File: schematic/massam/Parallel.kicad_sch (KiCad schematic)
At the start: 3 parts, among them J200 Conn_02x40_Row_Letter_First, U300 82C55A

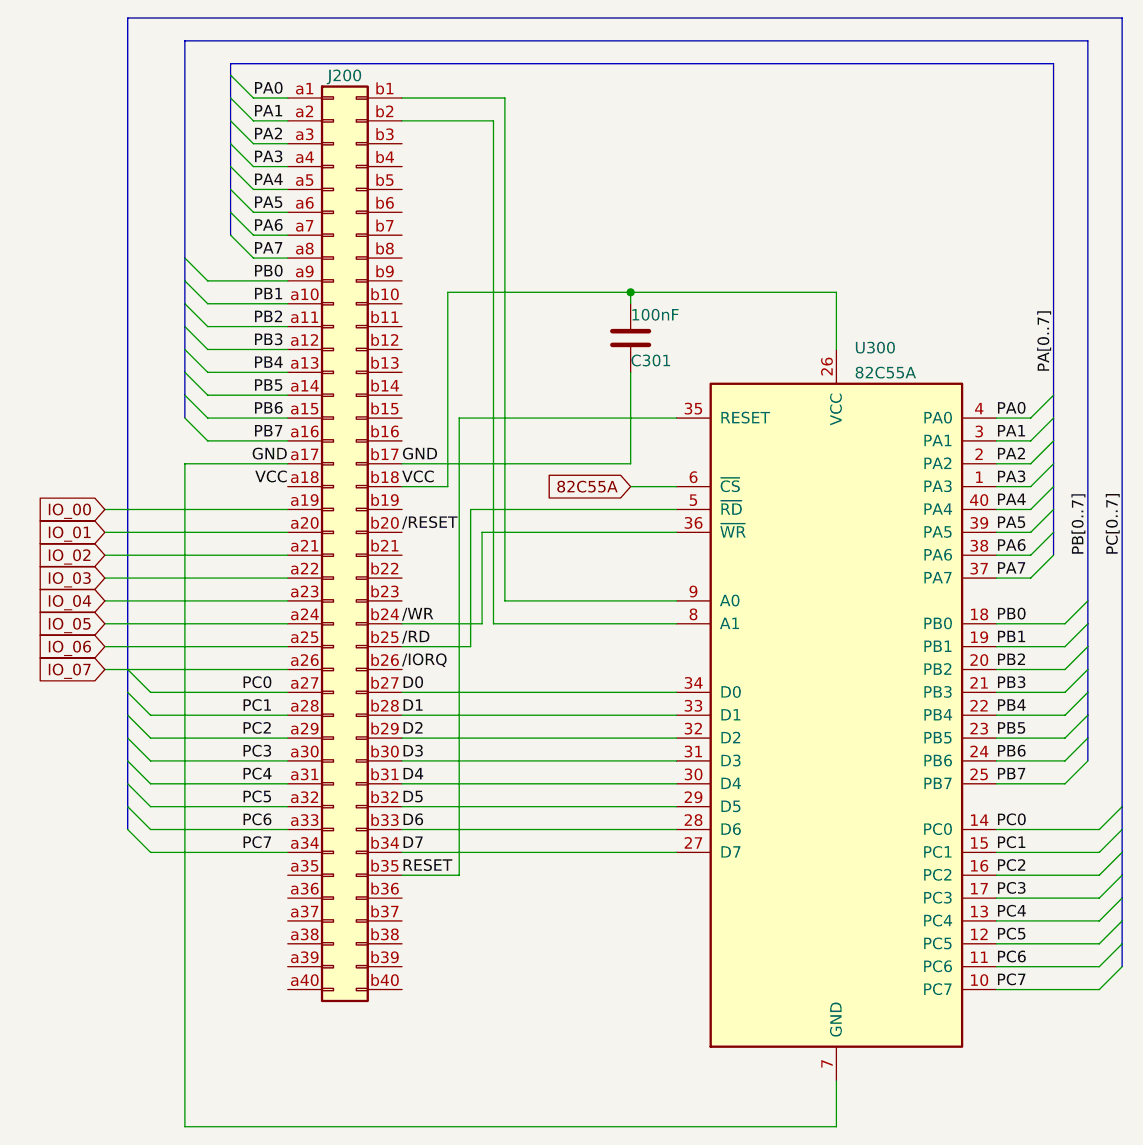
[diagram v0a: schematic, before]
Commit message: Added schematic for W65C02
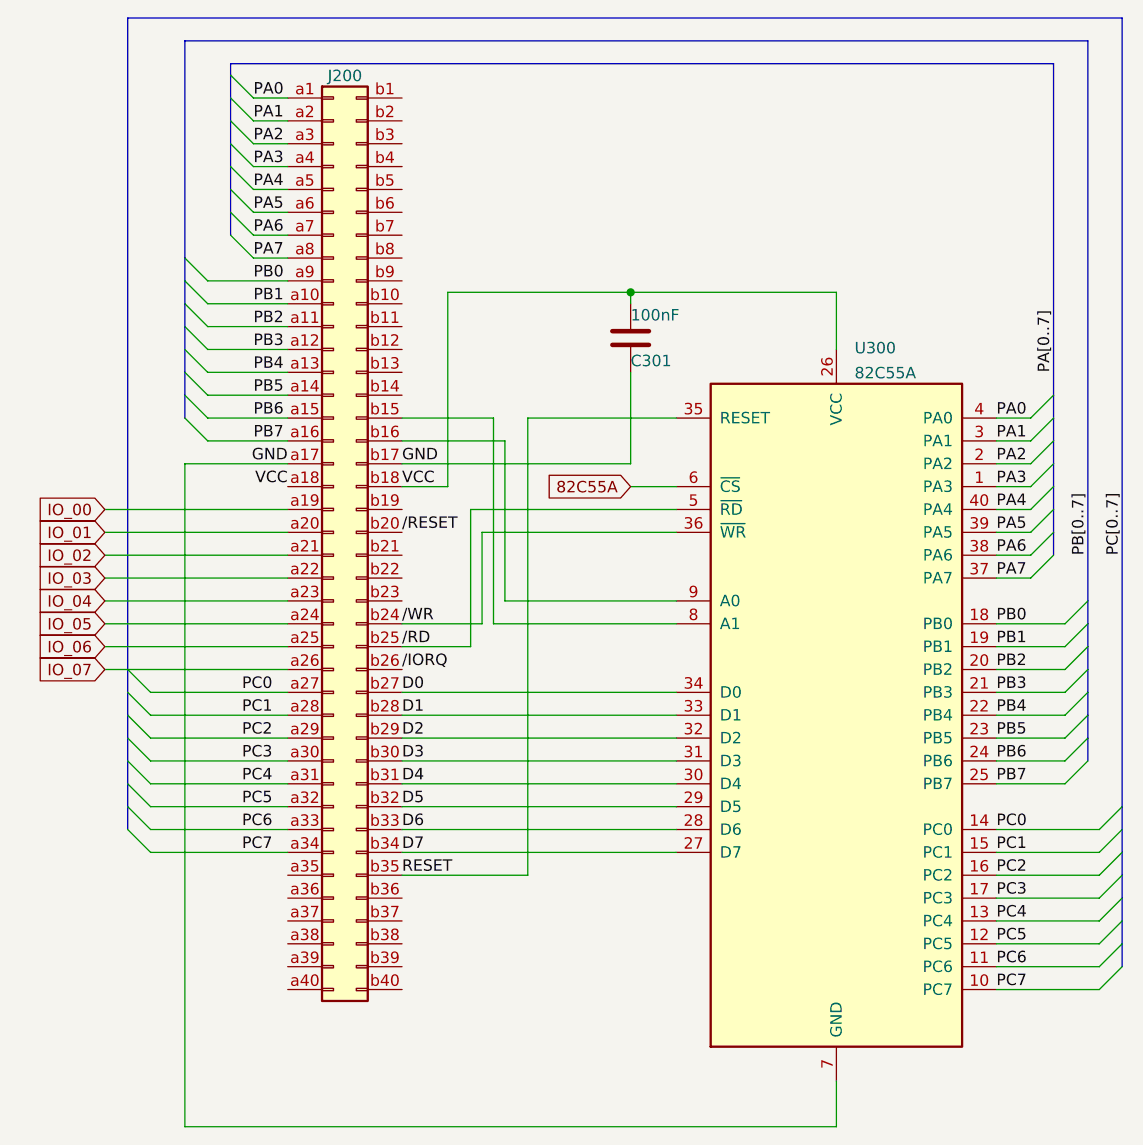
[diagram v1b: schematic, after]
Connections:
- net at U300.8 (A1): now also J200.b15 (Pin_b15); no longer J200.b2 (Pin_b2)
- net at U300.9 (A0): now also J200.b16 (Pin_b16); no longer J200.b1 (Pin_b1)
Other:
- title: SPARTAN -> HMC56
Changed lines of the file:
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@@
   (paper "A4")
   (title_block
-    (title "SPARTAN")
+    (title "HMC56")
     (rev "A")
     (company "Open Software")
-    (comment 1 "Retro computer SPARTAN using 65C02")
+    (comment 1 "Retro computer HMC56 using R6502")
     (comment 2 "Paulo da Silva (pdsilva)")
     (comment 3 "ppsilv gmail com")
@@
     (stroke (width 0) (type default) (color 0 0 0 0))
   )
+  (wire (pts (xy 57.15 62.23) (xy 68.58 62.23))
+    (stroke (width 0) (type default) (color 0 0 0 0))
+  )
   (wire (pts (xy 40.64 34.29) (xy 44.45 34.29))
     (stroke (width 0) (type default) (color 0 0 0 0))
@@
     (stroke (width 0) (type default) (color 0 0 0 0))
   )
+  (wire (pts (xy 67.31 82.55) (xy 67.31 59.69))
+    (stroke (width 0) (type default) (color 0 0 0 0))
+  )
   (wire (pts (xy 24.13 74.93) (xy 44.45 74.93))
     (stroke (width 0) (type default) (color 0 0 0 0))
   )
-  (wire (pts (xy 67.31 26.67) (xy 57.15 26.67))
-    (stroke (width 0) (type default) (color 0 0 0 0))
-  )
   (wire (pts (xy 29.21 90.17) (xy 44.45 90.17))
     (stroke (width 0) (type default) (color 0 0 0 0))
@@
     (stroke (width 0) (type default) (color 0 0 0 0))
   )
-  (wire (pts (xy 68.58 24.13) (xy 68.58 80.01))
-    (stroke (width 0) (type default) (color 0 0 0 0))
-  )
   (wire (pts (xy 82.55 64.77) (xy 82.55 54.61))
     (stroke (width 0) (type default) (color 0 0 0 0))
@@
     (stroke (width 0) (type default) (color 0 0 0 0))
   )
-  (wire (pts (xy 63.5 59.69) (xy 87.63 59.69))
+  (wire (pts (xy 71.12 59.69) (xy 87.63 59.69))
     (stroke (width 0) (type default) (color 0 0 0 0))
   )
@@
     (stroke (width 0) (type default) (color 0 0 0 0))
   )
-  (wire (pts (xy 67.31 82.55) (xy 67.31 26.67))
-    (stroke (width 0) (type default) (color 0 0 0 0))
-  )
-  (wire (pts (xy 57.15 110.49) (xy 63.5 110.49))
+  (wire (pts (xy 57.15 110.49) (xy 71.12 110.49))
     (stroke (width 0) (type default) (color 0 0 0 0))
   )
@@
     (stroke (width 0) (type default) (color 0 0 0 0))
   )
-  (wire (pts (xy 57.15 24.13) (xy 68.58 24.13))
-    (stroke (width 0) (type default) (color 0 0 0 0))
-  )
   (bus (pts (xy 137.16 113.03) (xy 137.16 110.49))
     (stroke (width 0) (type default) (color 0 0 0 0))
@@
     (stroke (width 0) (type default) (color 0 0 0 0))
   )
+  (wire (pts (xy 68.58 62.23) (xy 68.58 80.01))
+    (stroke (width 0) (type default) (color 0 0 0 0))
+  )
   (bus (pts (xy 38.1 20.32) (xy 129.54 20.32))
     (stroke (width 0) (type default) (color 0 0 0 0))
@@
     (stroke (width 0) (type default) (color 0 0 0 0))
   )
+  (wire (pts (xy 57.15 59.69) (xy 67.31 59.69))
+    (stroke (width 0) (type default) (color 0 0 0 0))
+  )
   (wire (pts (xy 66.04 72.39) (xy 87.63 72.39))
     (stroke (width 0) (type default) (color 0 0 0 0))
@@
     (stroke (width 0) (type default) (color 0 0 0 0))
   )
-  (wire (pts (xy 63.5 59.69) (xy 63.5 110.49))
-    (stroke (width 0) (type default) (color 0 0 0 0))
-  )
+  (wire (pts (xy 71.12 59.69) (xy 71.12 110.49))
+    (stroke (width 0) (type default) (color 0 0 0 0))
+  )
